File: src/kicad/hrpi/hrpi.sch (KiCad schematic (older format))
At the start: 28 parts, among them P1 CONN_02X20, P10 CONN_01X01, P11 CONN_01X04, P12 CONN_01X05, P13 CONN_01X05, P14 CONN_01X05, P15 CONN_01X04, P16 CONN_01X04, P17 CONN_01X02, P2 CONN_02X04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

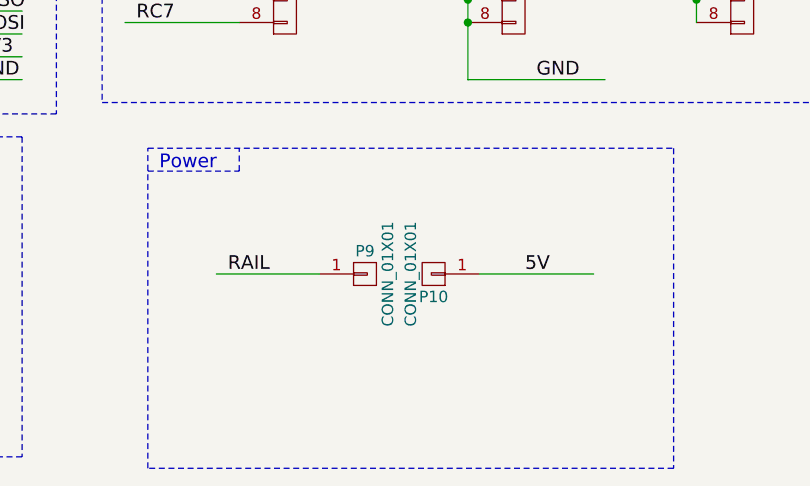
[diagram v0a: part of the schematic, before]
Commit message: Replaced power jumper
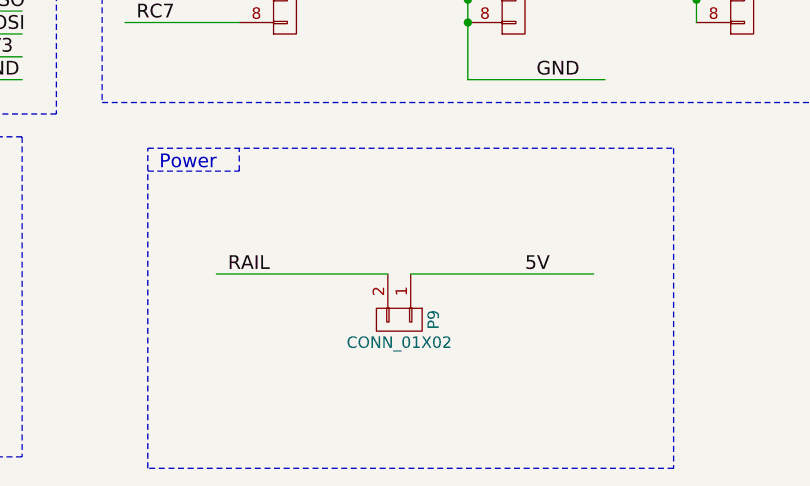
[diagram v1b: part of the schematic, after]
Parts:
- removed P10, P9: CONN_01X01, Pin_Headers:Pin_Header_Straight_1x01, symbol CONN_01X01
- added P9: CONN_01X02, Pin_Headers:Pin_Header_Straight_1x02, symbol CONN_01X02
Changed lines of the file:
@@
 EESchema Schematic File Version 2
+LIBS:valves
 LIBS:power
 LIBS:device
@@
 LIBS:atmel
 LIBS:contrib
-LIBS:valves
 LIBS:hrpi-cache
 EELAYER 25 0
@@
 Text Label 8250 4200 0    60   ~ 0
 5V
-$Comp
-L CONN_01X01 P9
-U 1 1 575C0076
-P 5850 5250
-F 0 "P9" H 5850 5350 50  0000 C CNN
-F 1 "CONN_01X01" V 5950 5250 50  0000 C CNN
-F 2 "Pin_Headers:Pin_Header_Straight_1x01" H 5850 5250 50  0001 C CNN
-F 3 "" H 5850 5250 50  0000 C CNN
-	1    5850 5250
-	1    0    0    -1
-$EndComp
-$Comp
-L CONN_01X01 P10
-U 1 1 575C011F
-P 6150 5250
-F 0 "P10" H 6150 5350 50  0000 C CNN
-F 1 "CONN_01X01" V 6250 5250 50  0000 C CNN
-F 2 "Pin_Headers:Pin_Header_Straight_1x01" H 6150 5250 50  0001 C CNN
-F 3 "" H 6150 5250 50  0000 C CNN
-	1    6150 5250
-	-1   0    0    1
-$EndComp
 Text Label 8250 3800 0    60   ~ 0
 SDA
@@
 Connection ~ 7300 3450
 Wire Wire Line
-	6350 5250 6850 5250
-Wire Wire Line
-	5200 5250 5650 5250
+	6050 5250 6850 5250
+Wire Wire Line
+	5200 5250 5950 5250
 Wire Wire Line
 	3000 1450 3400 1450
@@
 Text Label 4300 1700 0    60   ~ 0
 RCOK
+$Comp
+L CONN_01X02 P9
+U 1 1 57755189
+P 6000 5450
+F 0 "P9" H 6000 5600 50  0000 C CNN
+F 1 "CONN_01X02" V 6100 5450 50  0000 C CNN
+F 2 "Pin_Headers:Pin_Header_Straight_1x02" H 6000 5450 50  0001 C CNN
+F 3 "" H 6000 5450 50  0000 C CNN
+	1    6000 5450
+	0    1    1    0
+$EndComp
 $EndSCHEMATC
